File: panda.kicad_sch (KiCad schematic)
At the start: 5 parts

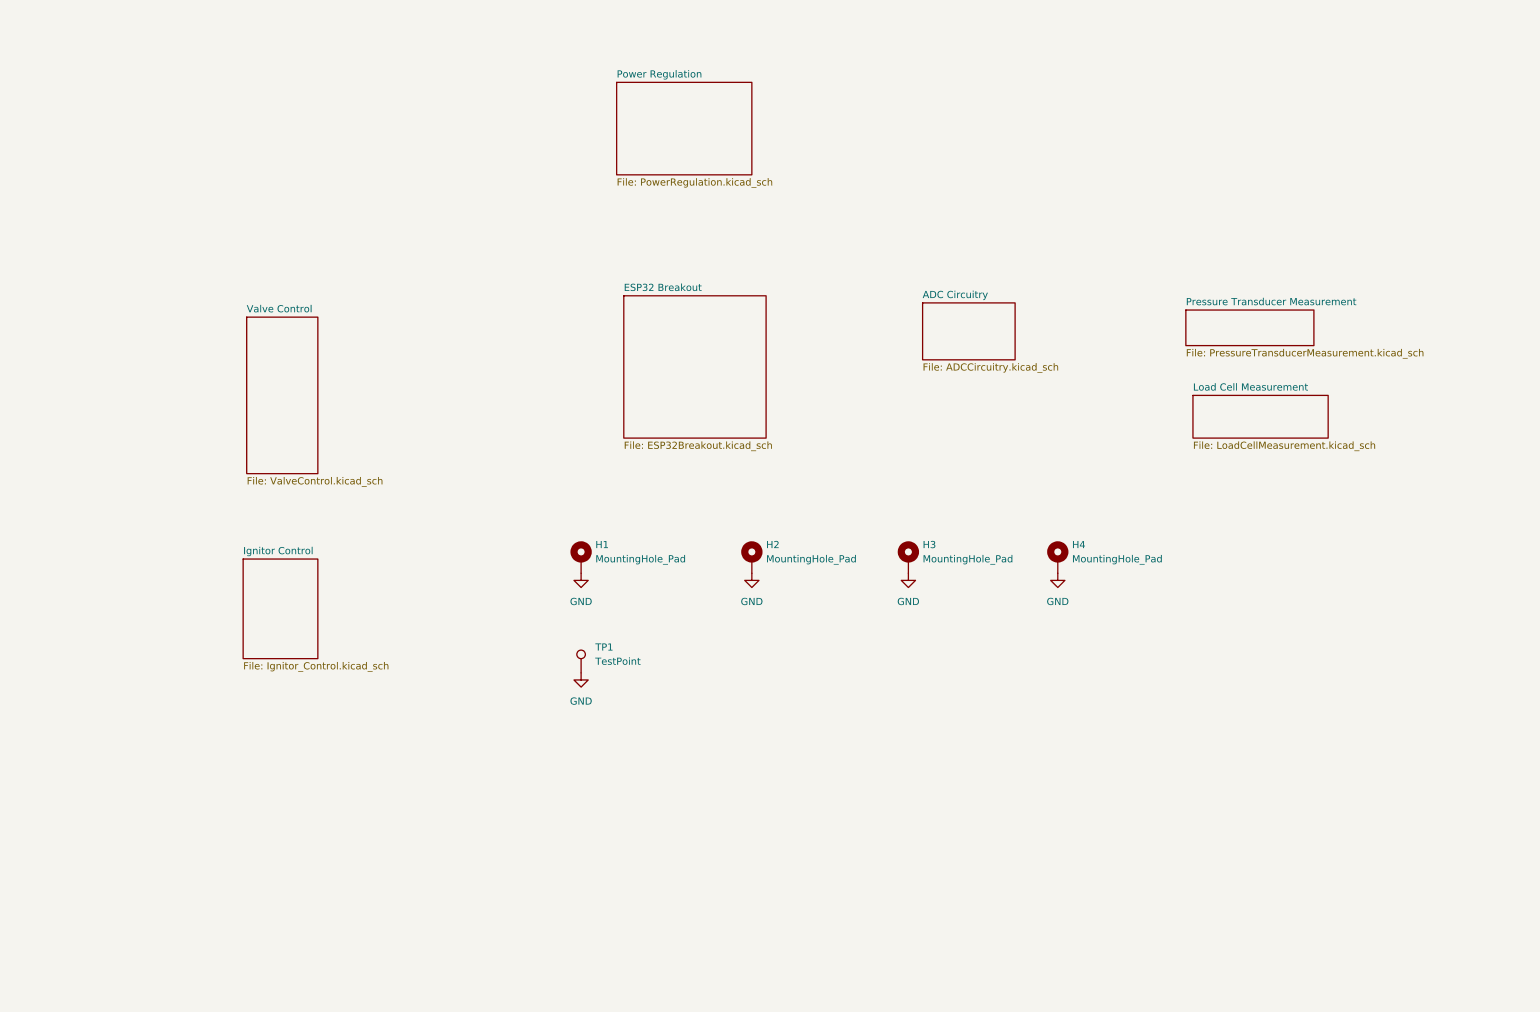
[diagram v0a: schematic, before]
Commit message: revamped schematic to be more readable
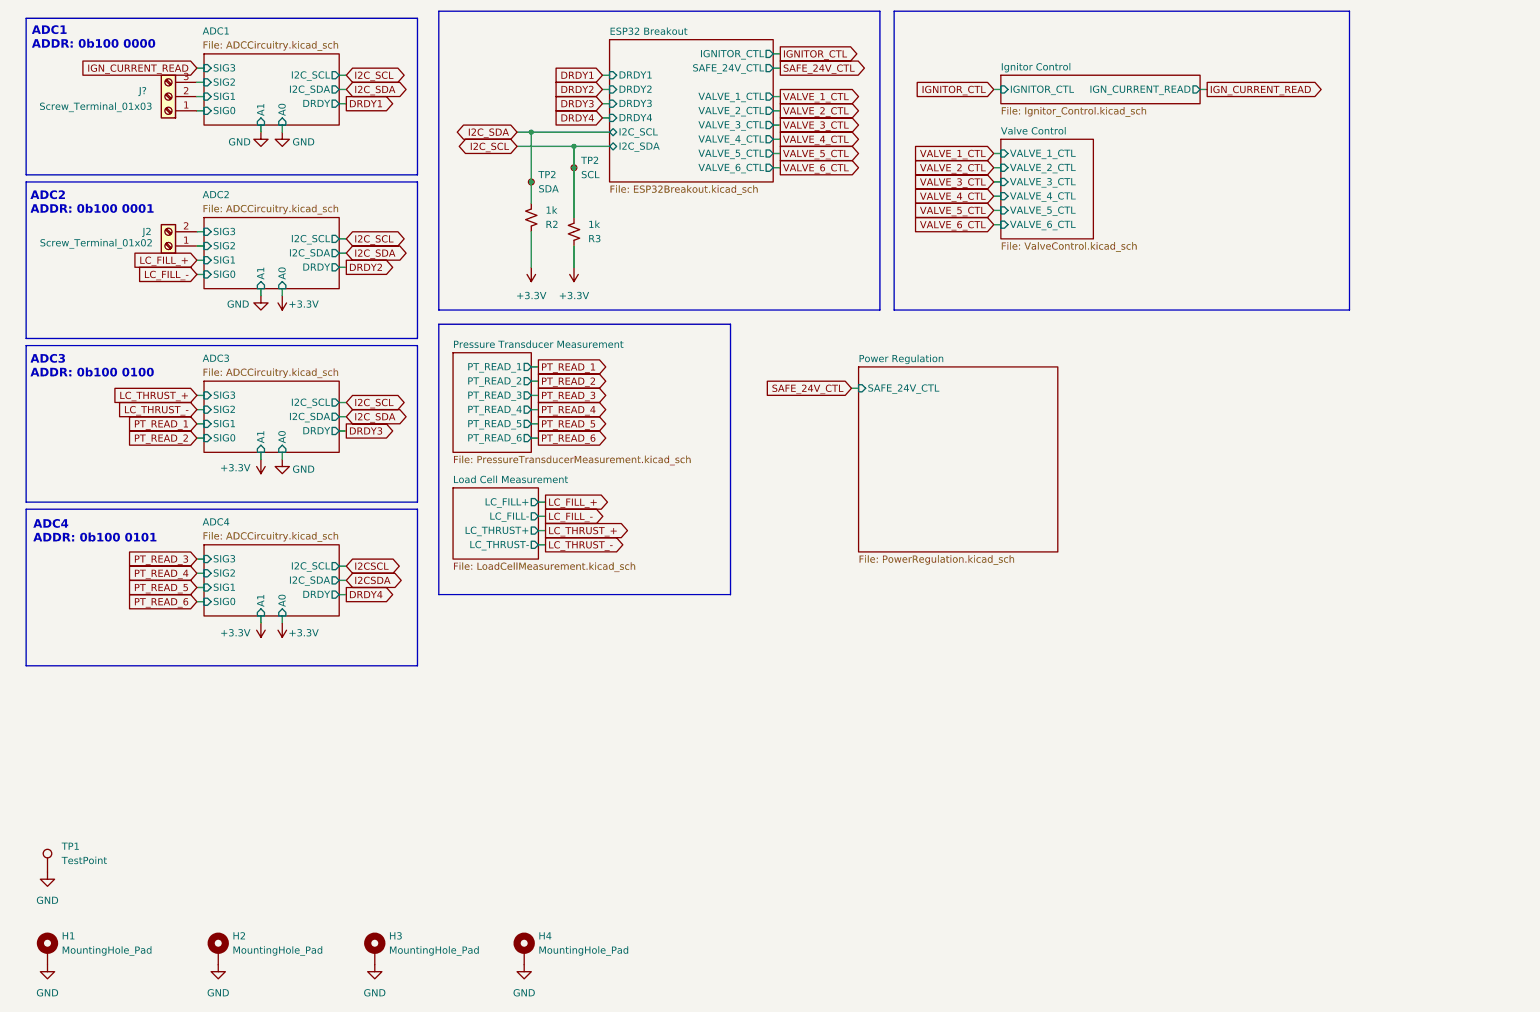
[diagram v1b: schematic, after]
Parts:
- added J2: Screw_Terminal_01x02, TerminalBlock:TerminalBlock_Xinya_XY308-2.54-2P_1x02_P2.54mm_Horizontal, symbol Connector:Screw_Terminal_01x02
- added J?: Screw_Terminal_01x03, TerminalBlock:TerminalBlock_Xinya_XY308-2.54-3P_1x03_P2.54mm_Horizontal, symbol Connector:Screw_Terminal_01x03
- added R2, R3: 1k, Resistor_SMD:R_0402_1005Metric, symbol Device:R_Small_US
- added TP2: SDA, TestPoint:TestPoint_Pad_D1.5mm, symbol Connector:TestPoint_Small
- added TP2: SCL, TestPoint:TestPoint_Pad_D1.5mm, symbol Connector:TestPoint_Small
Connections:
- new net +3.3V: R2.1, R3.1
- new net ADC1/SIG0: J?.1 (Pin_1)
- new net ADC1/SIG1: J?.2 (Pin_2)
- new net ADC1/SIG2: J?.3 (Pin_3)
- new net ADC2/SIG2: J2.1 (Pin_1)
- new net ADC2/SIG3: J2.2 (Pin_2)
- new net I2C_SCL: R3.2, TP2.1
- new net I2C_SDA: R2.2, TP2.1
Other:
- sheet ADC Circuitry renamed ADC1
- added sheet ADC2 (ADCCircuitry.kicad_sch)
- added sheet ADC3 (ADCCircuitry.kicad_sch)
- added sheet ADC4 (ADCCircuitry.kicad_sch)
- sheet ADC1 ports: added A0, A1, DRDY, I2C_SCL, I2C_SDA, SIG0, SIG1, SIG2, SIG3; removed none
- sheet ESP32 Breakout ports: added DRDY1, DRDY2, DRDY3, DRDY4, I2C_SCL, I2C_SDA, IGNITOR_CTL, SAFE_24V_CTL, VALVE_1_CTL, VALVE_2_CTL, VALVE_3_CTL, VALVE_4_CTL, VALVE_5_CTL, VALVE_6_CTL; removed none
- sheet Ignitor Control ports: added IGNITOR_CTL, IGN_CURRENT_READ; removed none
- sheet Load Cell Measurement ports: added LC_FILL+, LC_FILL-, LC_THRUST+, LC_THRUST-; removed none
- sheet Power Regulation ports: added SAFE_24V_CTL; removed none
- sheet Pressure Transducer Measurement ports: added PT_READ_1, PT_READ_2, PT_READ_3, PT_READ_4, PT_READ_5, PT_READ_6; removed none
- sheet Valve Control ports: added VALVE_1_CTL, VALVE_2_CTL, VALVE_3_CTL, VALVE_4_CTL, VALVE_5_CTL, VALVE_6_CTL; removed none
- note added: "ADC1 ADDR: 0b100 0000"
- note added: "ADC2 ADDR: 0b100 0001"
- note added: "ADC3 ADDR: 0b100 0100"
- note added: "ADC4 ADDR: 0b100 0101"
- moved on the sheet: H1, H2, H3, H4, TP1

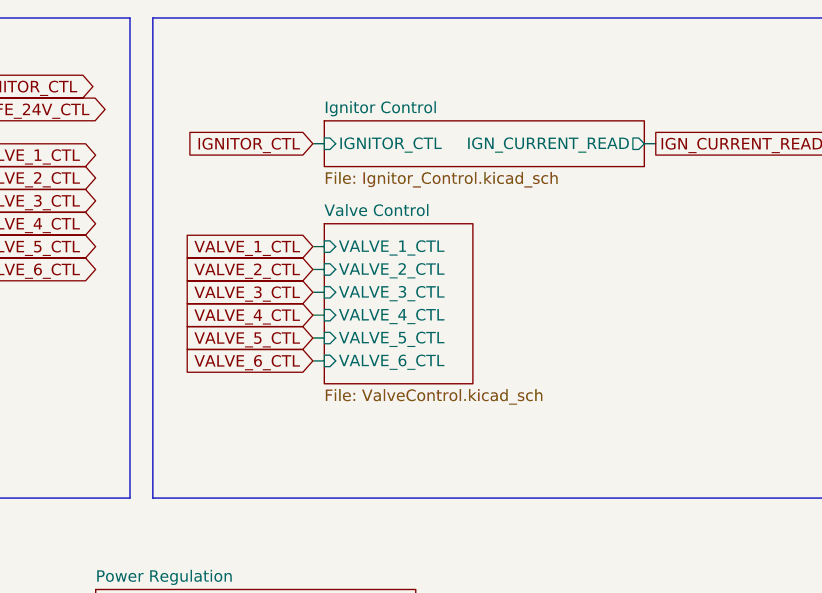
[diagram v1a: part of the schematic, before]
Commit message: remove diode between 5V and 5V_USB due to oversight (ADS112C04 cannot have DVDD without AVDD)
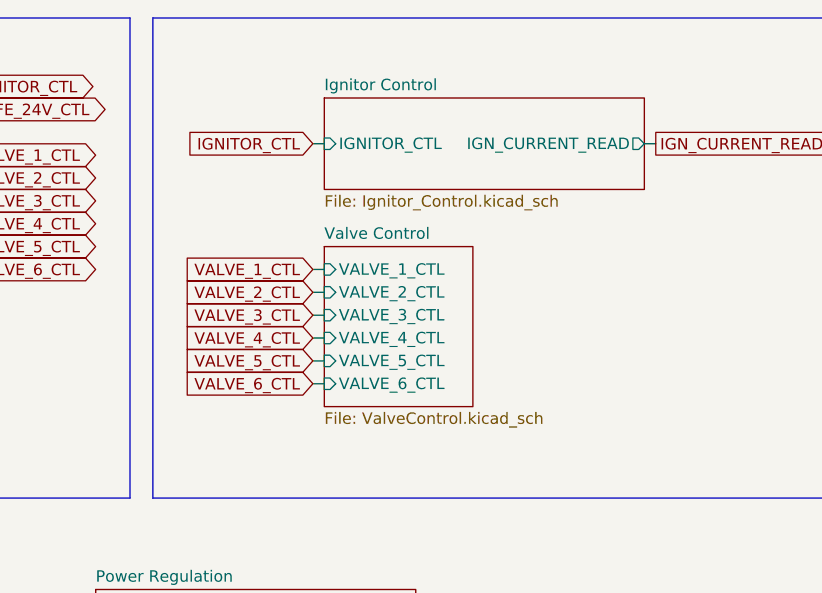
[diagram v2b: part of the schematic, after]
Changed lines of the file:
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@@
 	(wire
 		(pts
-			(xy 189.23 52.07) (xy 190.5 52.07)
+			(xy 189.23 54.61) (xy 190.5 54.61)
 		)
 		(stroke
@@
 	(wire
 		(pts
-			(xy 189.23 54.61) (xy 190.5 54.61)
+			(xy 189.23 57.15) (xy 190.5 57.15)
 		)
 		(stroke
@@
 	(wire
 		(pts
-			(xy 189.23 41.91) (xy 190.5 41.91)
+			(xy 189.23 44.45) (xy 190.5 44.45)
 		)
 		(stroke
@@
 	(wire
 		(pts
-			(xy 189.23 46.99) (xy 190.5 46.99)
+			(xy 189.23 49.53) (xy 190.5 49.53)
 		)
 		(stroke
@@
 	(wire
 		(pts
-			(xy 189.23 44.45) (xy 190.5 44.45)
+			(xy 189.23 46.99) (xy 190.5 46.99)
 		)
 		(stroke
@@
 	(wire
 		(pts
-			(xy 189.23 49.53) (xy 190.5 49.53)
+			(xy 189.23 52.07) (xy 190.5 52.07)
 		)
 		(stroke
@@
 	(global_label "VALVE_1_CTL"
 		(shape input)
-		(at 189.23 41.91 180)
+		(at 189.23 44.45 180)
 		(fields_autoplaced yes)
 		(effects
@@
 		)
 		(property "Intersheetrefs" "${INTERSHEET_REFS}"
-			(at 174.3915 41.91 0)
+			(at 174.3915 44.45 0)
 			(effects
 				(font
@@
 	(global_label "VALVE_4_CTL"
 		(shape input)
-		(at 189.23 49.53 180)
+		(at 189.23 52.07 180)
 		(fields_autoplaced yes)
 		(effects
@@
 		)
 		(property "Intersheetrefs" "${INTERSHEET_REFS}"
-			(at 174.3915 49.53 0)
+			(at 174.3915 52.07 0)
 			(effects
 				(font
@@
 	(global_label "VALVE_5_CTL"
 		(shape input)
-		(at 189.23 52.07 180)
+		(at 189.23 54.61 180)
 		(fields_autoplaced yes)
 		(effects
@@
 		)
 		(property "Intersheetrefs" "${INTERSHEET_REFS}"
-			(at 174.3915 52.07 0)
+			(at 174.3915 54.61 0)
 			(effects
 				(font
@@
 	(global_label "VALVE_6_CTL"
 		(shape input)
-		(at 189.23 54.61 180)
+		(at 189.23 57.15 180)
 		(fields_autoplaced yes)
 		(effects
@@
 		)
 		(property "Intersheetrefs" "${INTERSHEET_REFS}"
-			(at 174.3915 54.61 0)
+			(at 174.3915 57.15 0)
 			(effects
 				(font
@@
 	(global_label "VALVE_3_CTL"
 		(shape input)
-		(at 189.23 46.99 180)
+		(at 189.23 49.53 180)
 		(fields_autoplaced yes)
 		(effects
@@
 		)
 		(property "Intersheetrefs" "${INTERSHEET_REFS}"
-			(at 174.3915 46.99 0)
+			(at 174.3915 49.53 0)
 			(effects
 				(font
@@
 	(global_label "VALVE_2_CTL"
 		(shape input)
-		(at 189.23 44.45 180)
+		(at 189.23 46.99 180)
 		(fields_autoplaced yes)
 		(effects
@@
 		)
 		(property "Intersheetrefs" "${INTERSHEET_REFS}"
-			(at 174.3915 44.45 0)
+			(at 174.3915 46.99 0)
 			(effects
 				(font
@@
 	)
 	(sheet
-		(at 190.5 27.94)
-		(size 35.56 5.08)
+		(at 190.5 25.4)
+		(size 35.56 10.16)
 		(exclude_from_sim no)
 		(in_bom yes)
@@
 		)
 		(property "Sheetname" "Ignitor Control"
-			(at 190.5 27.2284 0)
+			(at 190.5 24.6884 0)
 			(effects
 				(font
@@
 		)
 		(property "Sheetfile" "Ignitor_Control.kicad_sch"
-			(at 190.5 33.6046 0)
+			(at 190.5 36.1446 0)
 			(effects
 				(font
@@
 	)
 	(sheet
-		(at 190.5 39.37)
+		(at 190.5 41.91)
 		(size 16.51 17.78)
 		(exclude_from_sim no)
@@
 		)
 		(property "Sheetname" "Valve Control"
-			(at 190.5 38.6584 0)
+			(at 190.5 41.1984 0)
 			(effects
 				(font
@@
 		)
 		(property "Sheetfile" "ValveControl.kicad_sch"
-			(at 190.5 57.7346 0)
+			(at 190.5 60.2746 0)
 			(effects
 				(font
@@
 		)
 		(pin "VALVE_1_CTL" input
-			(at 190.5 41.91 180)
+			(at 190.5 44.45 180)
 			(effects
 				(font
@@
 		)
 		(pin "VALVE_2_CTL" input
-			(at 190.5 44.45 180)
+			(at 190.5 46.99 180)
 			(effects
 				(font
@@
 		)
 		(pin "VALVE_3_CTL" input
-			(at 190.5 46.99 180)
+			(at 190.5 49.53 180)
 			(effects
 				(font
@@
 		)
 		(pin "VALVE_4_CTL" input
-			(at 190.5 49.53 180)
+			(at 190.5 52.07 180)
 			(effects
 				(font
@@
 		)
 		(pin "VALVE_5_CTL" input
-			(at 190.5 52.07 180)
+			(at 190.5 54.61 180)
 			(effects
 				(font
@@
 		)
 		(pin "VALVE_6_CTL" input
-			(at 190.5 54.61 180)
+			(at 190.5 57.15 180)
 			(effects
 				(font

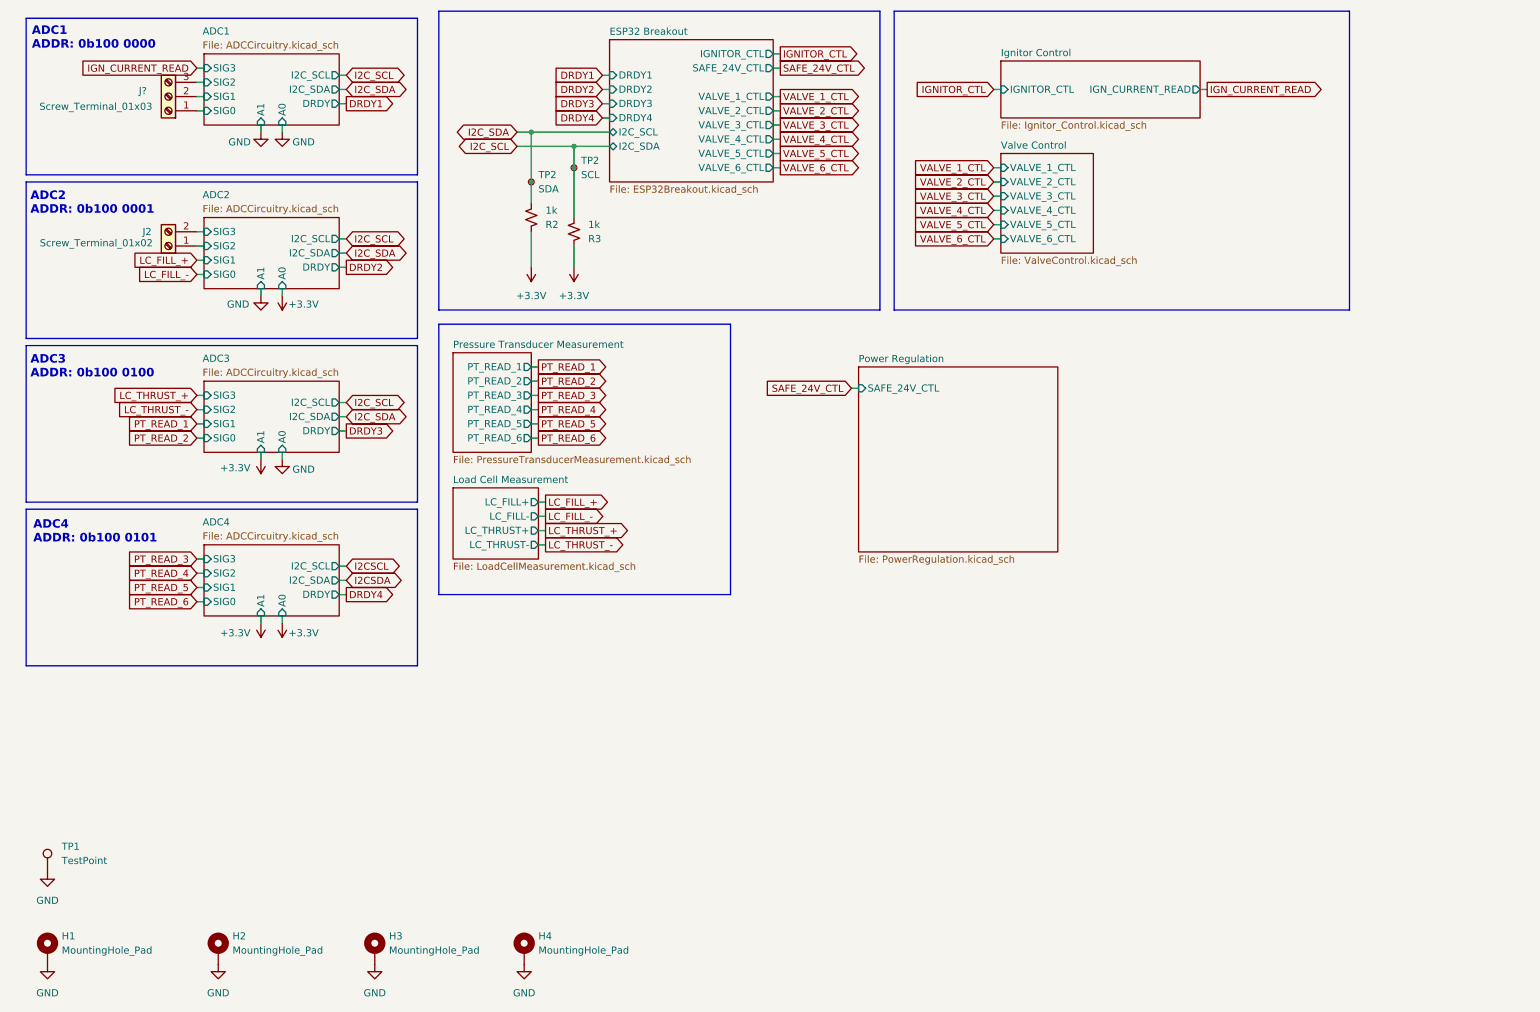
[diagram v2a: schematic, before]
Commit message: add thermocouple filtering, add 5th ADC
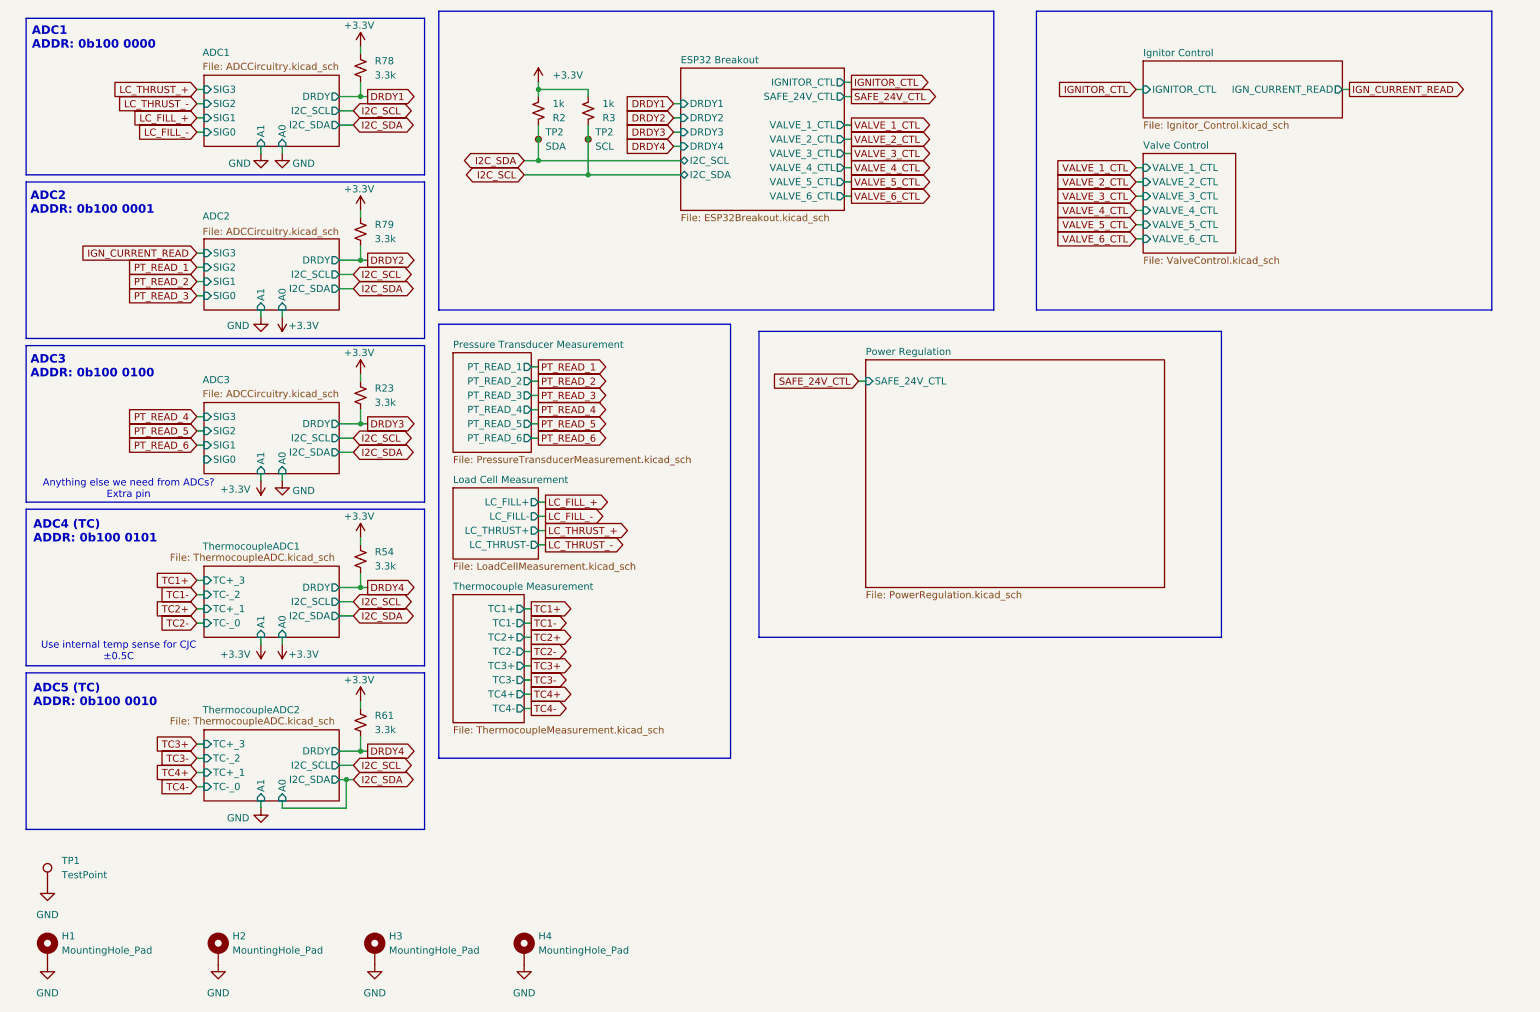
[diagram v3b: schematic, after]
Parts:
- removed J2: Screw_Terminal_01x02, TerminalBlock:TerminalBlock_Xinya_XY308-2.54-2P_1x02_P2.54mm_Horizontal, symbol Connector:Screw_Terminal_01x02
- removed J?: Screw_Terminal_01x03, TerminalBlock:TerminalBlock_Xinya_XY308-2.54-3P_1x03_P2.54mm_Horizontal, symbol Connector:Screw_Terminal_01x03
- added R23, R54, R61, R78, R79: 3.3k, Resistor_SMD:R_0402_1005Metric, symbol Device:R_Small_US
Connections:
- net +3.3V: now also R2.2, R3.2, R23.1, R54.1, R61.1, R78.1, R79.1; no longer R2.1, R3.1
- net DRDY1: now also R78.2
- net DRDY2: now also R79.2
- net DRDY3: now also R23.2
- net DRDY4: now also R54.2, R61.2
- net I2C_SCL: now also R3.1; no longer R3.2
- net I2C_SDA: now also R2.1; no longer R2.2
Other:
- removed sheet ADC4
- added sheet Thermocouple Measurement (ThermocoupleMeasurement.kicad_sch)
- added sheet ThermocoupleADC1 (ThermocoupleADC.kicad_sch)
- added sheet ThermocoupleADC2 (ThermocoupleADC.kicad_sch)
- note added: "ADC4 (TC) ADDR: 0b100 0101"
- note added: "ADC5 (TC) ADDR: 0b100 0010"
- note added: "Anything else we need from ADCs? Extra pin"
- note added: "Use internal temp sense for CJC ±0.5C"
- note removed: "ADC4 ADDR: 0b100 0101"
- moved on the sheet: R2, R3, TP1, TP2

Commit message: add 2 stage lockout to ignitor, add ignitor resistance reading with adc current source
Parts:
- renumbered R78 to R1, R79 to R2, R23 to R3, R54 to R4, R61 to R5, R2 to R6, R3 to R7, TP2 to TP3
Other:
- sheet ESP32 Breakout ports: added IGNITOR_PRIME_CTL, IGNITOR_RUN_CTL; removed IGNITOR_CTL
- sheet Ignitor Control ports: added IGNITOR_PRIME_CTL, IGNITOR_RUN_CTL, IGN_RESIST_READ; removed IGNITOR_CTL
- note added: "PGA 16x needed for IGN_RESIST_READ Reference PGA- to 2.048V internal reference ~5mOhm intervals"
- note removed: "Anything else we need from ADCs? Extra pin"
- moved on the sheet: TP1
